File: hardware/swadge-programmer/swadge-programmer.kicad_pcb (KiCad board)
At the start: 2 copper layers, 73.7 x 73.7 mm, 28 parts, among them J1 USB_B_Micro, J2 Conn_02x15_Top_Bottom, J3 Conn_02x15_Top_Bottom, J4 ftdi-header, J5 Conn_01x03_Male, SW1 4-1437565-2, SW2 4-1437565-2, SW3 4-1437565-2, SW4 SW_DPDT_x2, SW5 SW_DPDT_x2, U1 BUS_PCIexpress, U2 CP2102N-A01-GQFN24

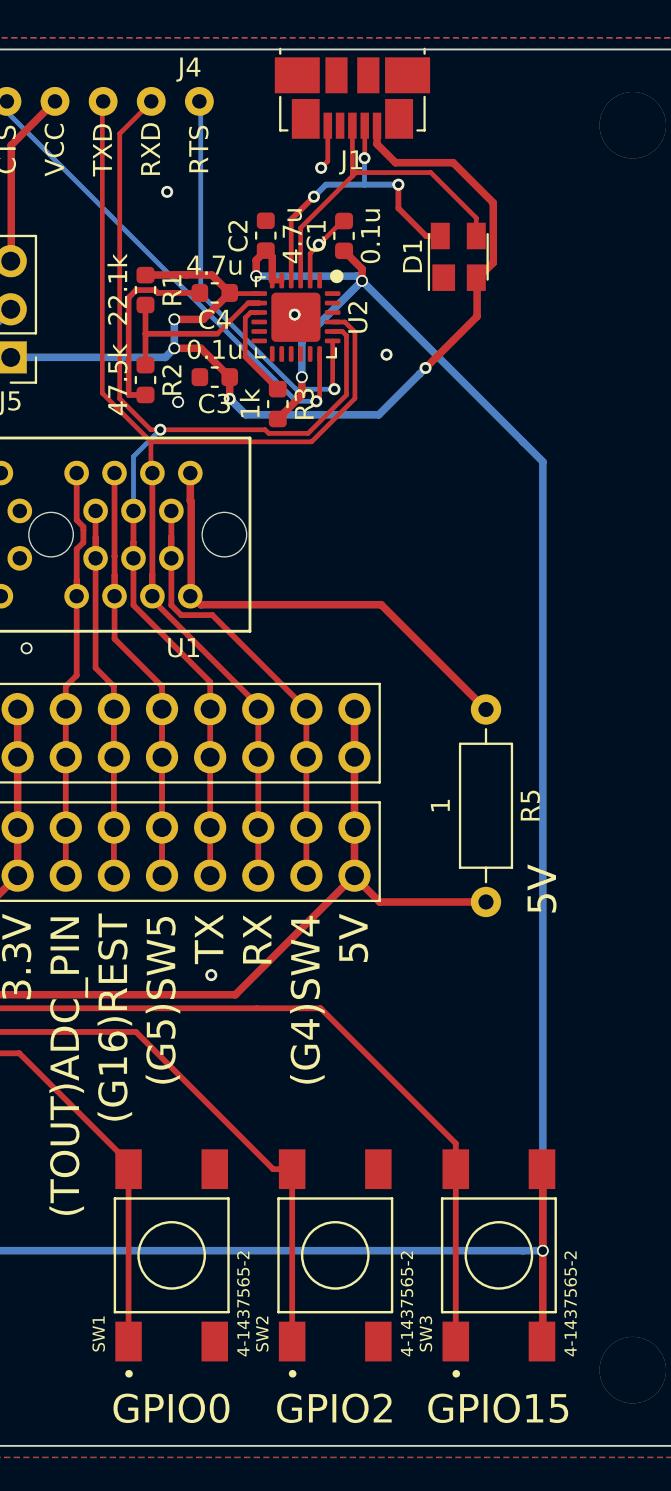
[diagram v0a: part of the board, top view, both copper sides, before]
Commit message: Fixed 3d model paths for all projects
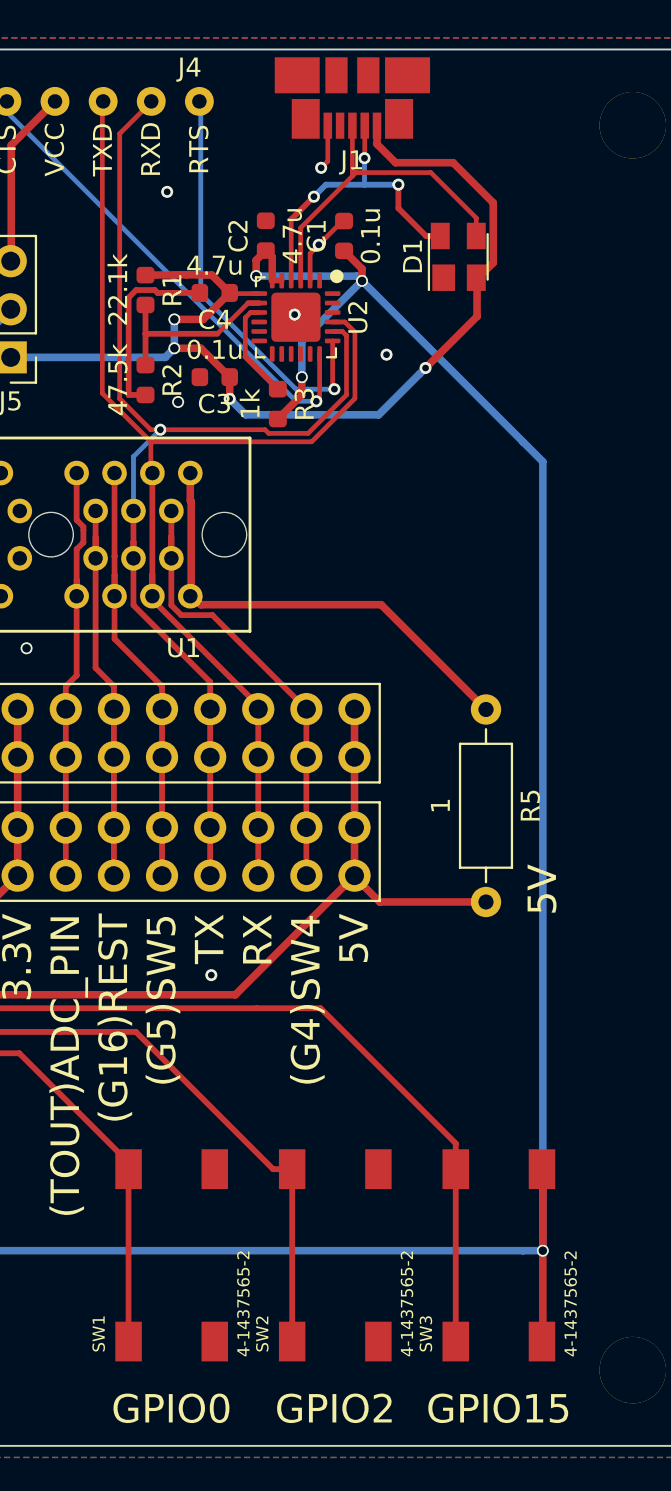
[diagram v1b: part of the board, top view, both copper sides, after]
